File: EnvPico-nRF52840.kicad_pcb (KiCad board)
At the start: 2 copper layers, 21.2 x 57.7 mm, 48 parts, among them J3 2.54mm header 01x20, J4 2.54mm header 01x20, J5 Conn_01x03_Male, U1 LM3671MF 3.3, U2 BQ24072RGT, U3 nRF52840, Y1 32MHz 12pF

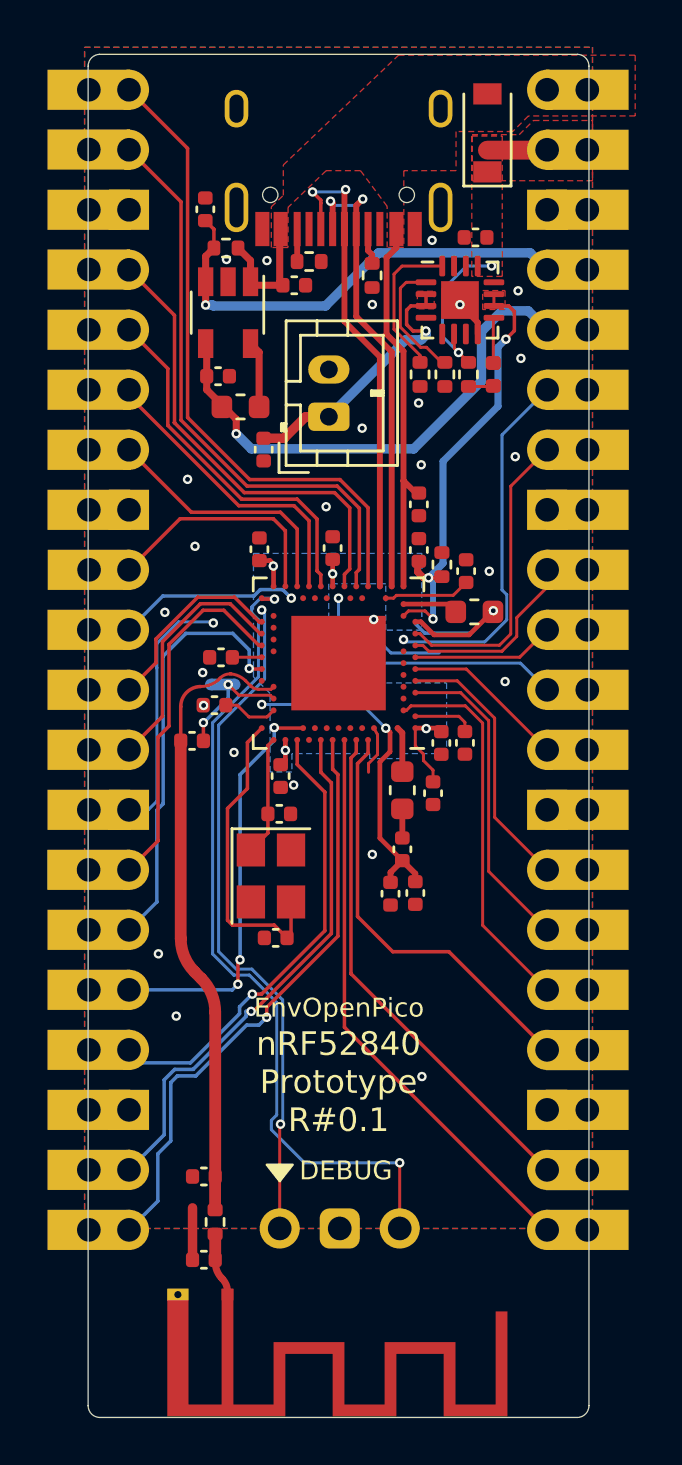
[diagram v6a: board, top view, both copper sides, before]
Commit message: I think this is correct trace thickness for 50ohm impedance
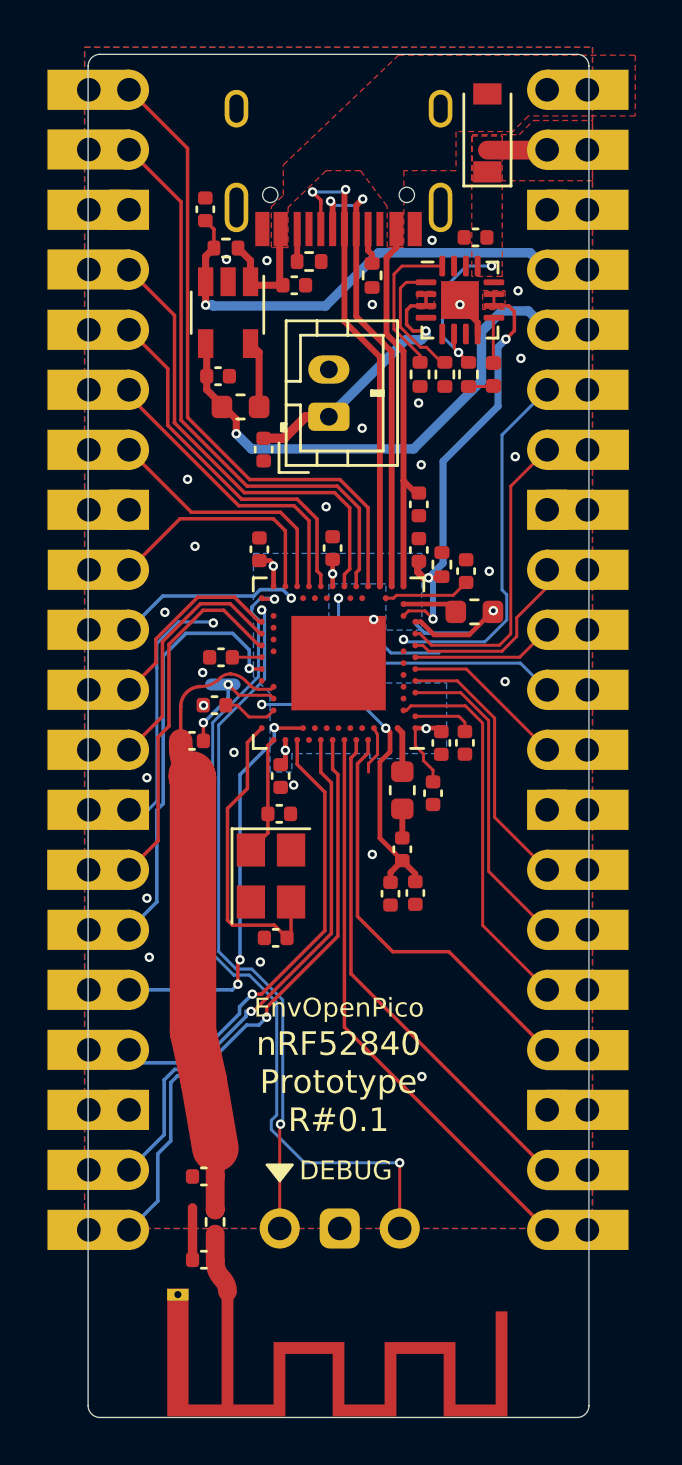
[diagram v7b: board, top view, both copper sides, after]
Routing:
- net GND: vias 27 -> 29
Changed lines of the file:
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@@
   (via (at 108.78 67.820822) (size 0.4) (drill 0.2) (layers "F.Cu" "B.Cu") (net 1))
   (via (at 111.36 70.095) (size 0.4) (drill 0.2) (layers "F.Cu" "B.Cu") (free) (net 1))
-  (via (at 96.015 95.3) (size 0.4) (drill 0.2) (layers "F.Cu" "B.Cu") (free) (net 1))
+  (via (at 100.33 95.645) (size 0.4) (drill 0.2) (layers "F.Cu" "B.Cu") (free) (net 1))
   (via (at 110.69 83.775) (size 0.4) (drill 0.2) (layers "F.Cu" "B.Cu") (free) (net 1))
   (via (at 96.29 80.845) (size 0.4) (drill 0.2) (layers "F.Cu" "B.Cu") (free) (net 1))
   (via (at 105.13 81.145) (size 0.4) (drill 0.2) (layers "F.Cu" "B.Cu") (net 1))
   (via (at 101.74 88.155) (size 0.4) (drill 0.2) (layers "F.Cu" "B.Cu") (free) (net 1))
+  (via (at 95.53 92.945) (size 0.4) (drill 0.2) (layers "F.Cu" "B.Cu") (free) (net 1))
   (via (at 107.6 65.095) (size 0.4) (drill 0.2) (layers "F.Cu" "B.Cu") (net 1))
-  (via (at 96.77 97.935) (size 0.4) (drill 0.2) (layers "F.Cu" "B.Cu") (free) (net 1))
   (via (at 107.14 74.6) (size 0.4) (drill 0.2) (layers "F.Cu" "B.Cu") (free) (net 1))
   (via (at 104.64 73.05) (size 0.4) (drill 0.2) (layers "F.Cu" "B.Cu") (free) (net 1))
@@
   (via (at 97.89 83.395) (size 0.4) (drill 0.2) (layers "F.Cu" "B.Cu") (net 1))
   (via (at 100.61 65.955) (size 0.4) (drill 0.2) (layers "F.Cu" "B.Cu") (net 1))
+  (via (at 95.53 87.845) (size 0.4) (drill 0.2) (layers "F.Cu" "B.Cu") (free) (net 1))
   (via (at 107.03 71.985) (size 0.4) (drill 0.2) (layers "F.Cu" "B.Cu") (net 1))
+  (via (at 95.63 95.445) (size 0.4) (drill 0.2) (layers "F.Cu" "B.Cu") (free) (net 1))
   (via (at 111.24 67.235) (size 0.4) (drill 0.2) (layers "F.Cu" "B.Cu") (free) (net 1))
   (via (at 103.115 76.375) (size 0.4) (drill 0.2) (layers "F.Cu" "B.Cu") (net 1))
@@
   (segment (start 108.04 69.165) (end 108.04 67.2) (width 0.127) (layer "B.Cu") (net 10))
   (segment (start 108.72 69.845) (end 108.04 69.165) (width 0.127) (layer "B.Cu") (net 10))
-  (segment (start 98.42 108.25) (end 98.42 107.165) (width 0.5) (layer "F.Cu") (net 11))
+  (segment (start 98.42 108.25) (end 98.42 107.165) (width 0.8) (layer "F.Cu") (net 11))
   (segment (start 98.42 108.25) (end 98.42 108.340786) (width 0.3) (layer "F.Cu") (net 11))
   (segment (start 98.42 107.165) (end 98.415 107.16) (width 0.5) (layer "F.Cu") (net 11))
   (segment (start 98.94 109.725) (end 98.94 109.596199) (width 0.3) (layer "F.Cu") (net 11))
-  (arc (start 98.42 108.340786) (mid 98.49612 108.723469) (end 98.712893 109.047893) (width 0.3) (layer "F.Cu") (net 11))
-  (arc (start 98.712893 109.047893) (mid 98.880974 109.29945) (end 98.94 109.596199) (width 0.3) (layer "F.Cu") (net 11))
+  (arc (start 98.42 108.340786) (mid 98.49612 108.723469) (end 98.712893 109.047893) (width 0.8) (layer "F.Cu") (net 11))
+  (arc (start 98.712893 109.047893) (mid 98.880974 109.29945) (end 98.94 109.596199) (width 0.8) (layer "F.Cu") (net 11))
   (segment (start 102.25 72.565) (end 101.34 73.475) (width 0.4) (layer "F.Cu") (net 12))
   (segment (start 106.52122 68.05178) (end 106.52122 68.661294) (width 0.15) (layer "F.Cu") (net 12))
@@
   (segment (start 99.31 73.285) (end 99.95 73.925) (width 0.4) (layer "B.Cu") (net 16))
   (segment (start 109.69 71.0552) (end 109.69 68.955) (width 0.4) (layer "B.Cu") (net 16))
+  (segment (start 97.43 87.795626) (end 97.43 87.705922) (width 1.968805) (layer "F.Cu") (net 17))
   (segment (start 100.89 83.995) (end 100.783531 84.101469) (width 0.127) (layer "F.Cu") (net 17))
+  (segment (start 98.42 104.725) (end 98.42 103.555) (width 0.8) (layer "F.Cu") (net 17))
   (segment (start 96.96 84.83779) (end 96.96 86.285) (width 0.15) (layer "F.Cu") (net 17))
-  (segment (start 98.415 106.14) (end 98.415 104.73) (width 0.5) (layer "F.Cu") (net 17))
+  (segment (start 97.93 100.645) (end 98.43 103.545) (width 1.968805) (layer "F.Cu") (net 17))
   (segment (start 98.6362 83.6188) (end 98.593292 83.661708) (width 0.127) (layer "F.Cu") (net 17))
-  (segment (start 98.42 104.725) (end 98.42 97.763427) (width 0.5) (layer "F.Cu") (net 17))
-  (segment (start 98.415 104.73) (end 98.42 104.725) (width 0.5) (layer "F.Cu") (net 17))
-  (segment (start 96.96 94.646573) (end 96.96 86.285) (width 0.5) (layer "F.Cu") (net 17))
+  (segment (start 97.48 87.845626) (end 97.48 98.595) (width 1.968805) (layer "F.Cu") (net 17))
+  (segment (start 98.42 104.725) (end 98.42 106.135) (width 0.8) (layer "F.Cu") (net 17))
   (segment (start 100.783531 84.101469) (end 100.258261 84.101469) (width 0.127) (layer "F.Cu") (net 17))
-  (segment (start 97.834213 96.349213) (end 97.545786 96.060786) (width 0.5) (layer "F.Cu") (net 17))
+  (segment (start 97.48 87.845626) (end 97.43 87.795626) (width 1.968805) (layer "F.Cu") (net 17))
+  (segment (start 98.42 106.135) (end 98.415 106.14) (width 0.8) (layer "F.Cu") (net 17))
   (segment (start 99.930851 83.965851) (end 99.707893 83.742893) (width 0.127) (layer "F.Cu") (net 17))
+  (segment (start 96.96 86.285) (end 96.96 86.590235) (width 1) (layer "F.Cu") (net 17))
   (segment (start 99.099056 83.45225) (end 99.038289 83.45225) (width 0.127) (layer "F.Cu") (net 17))
-  (arc (start 96.96 94.646573) (mid 97.112241 95.41194) (end 97.545786 96.060786) (width 0.5) (layer "F.Cu") (net 17))
+  (segment (start 97.48 98.595) (end 97.93 100.645) (width 1.968805) (layer "F.Cu") (net 17))
+  (segment (start 98.42 103.555) (end 98.43 103.545) (width 0.8) (layer "F.Cu") (net 17))
+  (arc (start 96.96 86.590235) (mid 97.095144 87.269647) (end 97.48 87.845626) (width 1) (layer "F.Cu") (net 17))
   (arc (start 98.6362 83.6188) (mid 98.82068 83.495534) (end 99.038289 83.45225) (width 0.127) (layer "F.Cu") (net 17))
   (arc (start 97.812797 83.985) (mid 98.235198 83.900979) (end 98.593292 83.661708) (width 0.127) (layer "F.Cu") (net 17))
-  (arc (start 97.834213 96.349213) (mid 98.267759 96.99806) (end 98.42 97.763427) (width 0.5) (layer "F.Cu") (net 17))
   (arc (start 100.258261 84.101469) (mid 100.081068 84.066223) (end 99.930851 83.965851) (width 0.127) (layer "F.Cu") (net 17))
   (arc (start 96.96 84.83779) (mid 97.209776 84.234776) (end 97.812797 83.985) (width 0.15) (layer "F.Cu") (net 17))
